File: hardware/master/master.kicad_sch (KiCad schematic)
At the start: 29 parts, among them J1 5V IN, J2 BUS OUT, J3 IO RSV, J4 STEP-UP 5V->15V, U1 ESP32-C3 SuperMini, U2 TP8485E-SR, U3 74LVC1G17

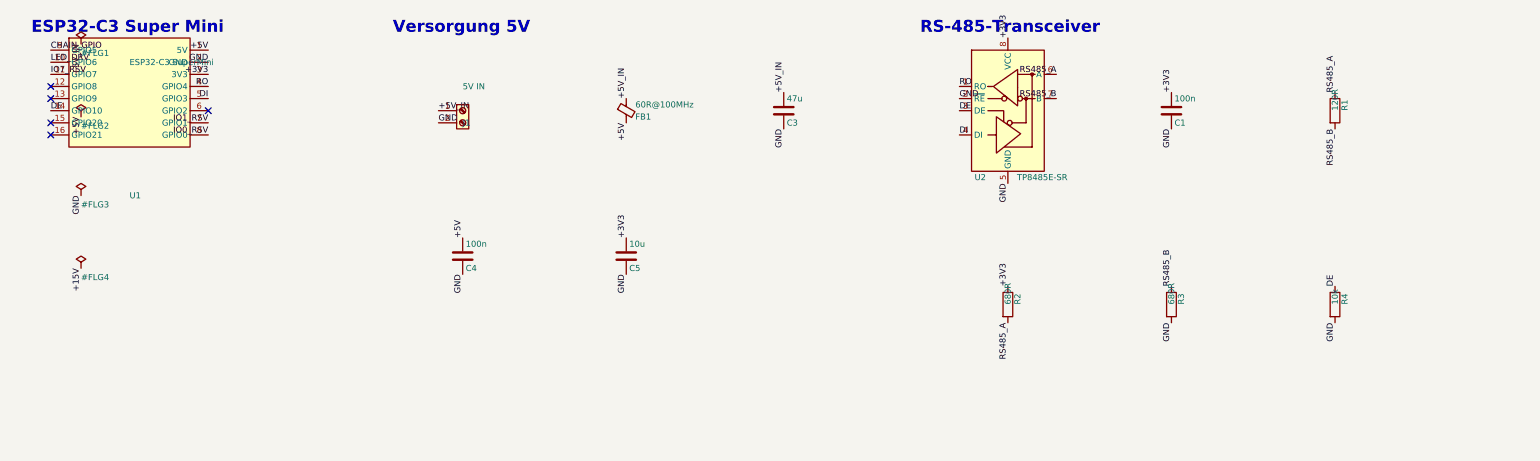
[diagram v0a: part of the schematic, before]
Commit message: Master-Traegerboard Rev. 0.2: Verpolschutz + RS-485-TVS am Eingang
Vor der PCB-Bestellung nachgeruestet (Betreiber-Entscheidungen 10.09.2026):

- Q1 (AO3401A, P-Kanal, High-Side) + R8 (100k V_GS) = Verpolschutz am
  5-V-Eingang, direkt hinter J1 und VOR der J2-Abzweigung -> schuetzt bei
  vertauschter Klemme die gesamte Kette. Neues Netz +5V_RAW (J1->Q1).
- D2 (SM712 / PSM712-LF-T7) = RS-485-TVS-Array zwischen A/B und GND,
  7 V / 12 V asymmetrisch (RS-485-Gleichtakt -7..+12 V). Pinbelegung gegen
  das Bourns-CDSOT23-SM712-Datenblatt geprueft (Pin 3 = GND).
- Alle drei sind LCSC-Basic-Teile: C15127, C149504, C32677.
- M-3 entschieden: U3 (74LVC1G17) wird bestueckt, R7 (0R) bleibt DNP-Reserve.
- Keine Edge.Cuts-Aussparung fuer U1 -- das Modul steckt in Buchsenleisten
  und wird zum Flashen entnommen.
- 5-V- und 42-V~-Kreis bleiben vollstaendig galvanisch getrennt (eigenes
  5-V-Netzteil, kein gemeinsamer Trafo, 5 V nicht aus den 42 V~).

Werkzeuge:
- build_krone_master_symbols.py: AO3401A + SM712_SOT23 aus der KiCad-Lib.
- gen_master_sch.py / gen_master_pcb.py: Q1/R8/D2 in Netzliste + PLACEMENT
  (PLACEMENT akzeptiert jetzt opt. Rueckseiten-Flag).
- tools/patch_master_pcb.py (neu): setzt neue Bauteile inkrementell in die
  geroutete Platine ein und schliesst nur die neuen Verbindungen mit
  finish_routes.py -- FreeRouting 2.3.0 haengt in dieser Umgebung reproduzierbar.
- route_master.py / route_daughtercard.py: -Dfreerouting.gui.enabled=false +
  Popen-Watchdog (.ses-Stabilitaet / CPU-Stillstand) + 3 Anlaeufe, --passes 6.

ERC 0/0, DRC 0/0. Schaltplan Rev. 0.2, Fertigungspaket regeneriert (18 SMD).
docs/schaltplan-master.md, symbolpruefung-master.md (AO3401A + SM712, M-4),
layout-master.md, spezifikation.md v0.21, backlog T20, projektstand, toolchain.

Co-Authored-By: Claude Sonnet 5 <noreply@anthropic.com>
Claude-Session: https://claude.ai/code/session_01UsXTvE3jGgoK5Hec7hVbyD
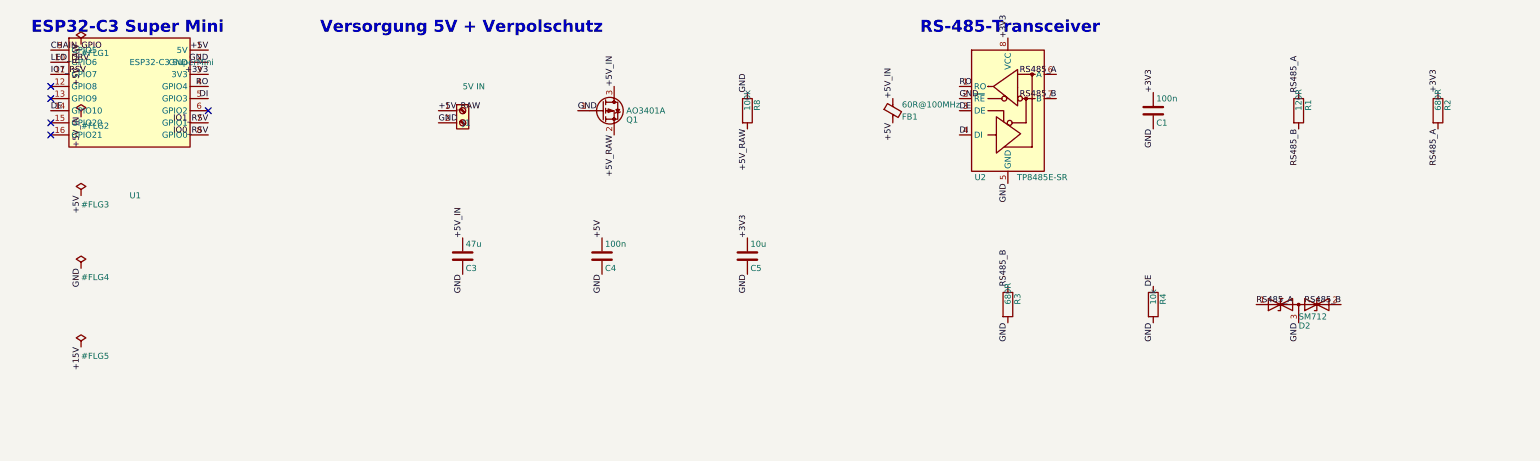
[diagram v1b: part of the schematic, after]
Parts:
- added D2: SM712, Package_TO_SOT_SMD:SOT-23, symbol krone_master:SM712_SOT23
- added Q1: AO3401A, Package_TO_SOT_SMD:SOT-23, symbol krone_master:AO3401A
- added R8: 100k, Resistor_SMD:R_0805_2012Metric, symbol krone_master:R
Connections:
- net +5V_IN: now also Q1.3 (D); no longer J1.1 (Pin_1)
- net GND: now also D2.3 (common), Q1.1 (G), R8.1
- net RS485_A: now also D2.1 (A1)
- net RS485_B: now also D2.2 (A2)
- new net +5V_RAW: J1.1 (Pin_1), Q1.2 (S), R8.2
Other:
- note added: "Versorgung 5V + Verpolschutz"
- note removed: "Versorgung 5V"
